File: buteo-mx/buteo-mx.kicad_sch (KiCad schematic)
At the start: 70 parts, among them J1 Conn_01x12_Pin, SW1 SW_SPST, SW10 SW_SPST, SW11 SW_SPST, SW12 SW_SPST, SW13 SW_SPST, SW14 SW_SPST, SW15 SW_SPST, SW16 SW_SPST, SW17 SW_SPST, SW18 SW_SPST, SW19 SW_SPST, SW2 SW_SPST, SW20 SW_SPST, SW21 SW_SPST, SW22 SW_SPST, SW23 SW_SPST, SW24 SW_SPST, SW25 SW_SPST, SW26 SW_SPST, SW27 SW_SPST, SW28 SW_SPST, SW29 SW_SPST, SW3 SW_SPST, SW30 SW_SPST, SW31 RotaryEncoder_Switch, SW4 SW_SPST, SW5 SW_SPST, SW6 SW_SPST, SW7 SW_SPST, SW8 SW_SPST, SW9 SW_SPST

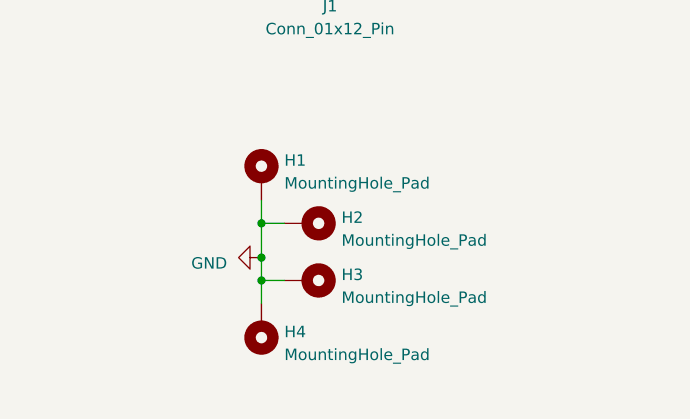
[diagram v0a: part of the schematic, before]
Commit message: Fix footprint references and 3D models
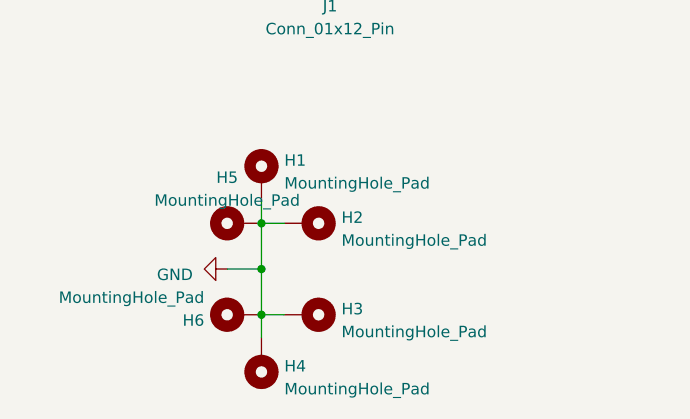
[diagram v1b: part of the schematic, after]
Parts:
- added H5, H6: MountingHole_Pad, MountingHole:MountingHole_2.2mm_M2_ISO7380_Pad_TopBottom, symbol Mechanical:MountingHole_Pad
- RZ1: footprint mcu:rp2040-zero-tht -> Pixelbreaker:rp2040-zero-tht
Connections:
- net GND: now also H5.1, H6.1
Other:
- moved on the sheet: H3, H4
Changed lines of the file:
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@@
   (junction (at 208.28 59.69) (diameter 0) (color 0 0 0 0)
   )
-  (junction (at 106.68 142.24) (diameter 0) (color 0 0 0 0)
-  )
   (junction (at 106.68 135.89) (diameter 0) (color 0 0 0 0)
   )
@@
   (junction (at 123.19 86.36) (diameter 0) (color 0 0 0 0)
   )
+  (junction (at 106.68 146.05) (diameter 0) (color 0 0 0 0)
+  )
   (junction (at 180.34 90.17) (diameter 0) (color 0 0 0 0)
   )
   (junction (at 170.18 85.09) (diameter 0) (color 0 0 0 0)
   )
-  (junction (at 106.68 139.7) (diameter 0) (color 0 0 0 0)
-  )
   (junction (at 218.44 64.77) (diameter 0) (color 0 0 0 0)
   )
@@
   (junction (at 180.34 102.87) (diameter 0) (color 0 0 0 0)
   )
+  (junction (at 106.68 140.97) (diameter 0) (color 0 0 0 0)
+  )
   (junction (at 218.44 39.37) (diameter 0) (color 0 0 0 0)
   )
@@
     (stroke (width 0) (type default))
   )
+  (wire (pts (xy 102.87 140.97) (xy 106.68 140.97))
+    (stroke (width 0) (type default))
+  )
   (wire (pts (xy 180.34 52.07) (xy 199.39 52.07))
     (stroke (width 0) (type default))
@@
     (stroke (width 0) (type default))
   )
-  (wire (pts (xy 106.68 142.24) (xy 109.22 142.24))
+  (wire (pts (xy 106.68 146.05) (xy 109.22 146.05))
     (stroke (width 0) (type default))
   )
@@
     (stroke (width 0) (type default))
   )
-  (wire (pts (xy 106.68 142.24) (xy 106.68 144.78))
-    (stroke (width 0) (type default))
-  )
   (wire (pts (xy 189.23 85.09) (xy 189.23 97.79))
     (stroke (width 0) (type default))
@@
     (stroke (width 0) (type default))
   )
+  (wire (pts (xy 106.68 140.97) (xy 106.68 146.05))
+    (stroke (width 0) (type default))
+  )
   (wire (pts (xy 170.18 34.29) (xy 170.18 46.99))
     (stroke (width 0) (type default))
@@
     (stroke (width 0) (type default))
   )
+  (wire (pts (xy 106.68 146.05) (xy 106.68 148.59))
+    (stroke (width 0) (type default))
+  )
   (wire (pts (xy 256.54 102.87) (xy 256.54 113.03))
     (stroke (width 0) (type default))
   )
-  (wire (pts (xy 106.68 135.89) (xy 106.68 139.7))
-    (stroke (width 0) (type default))
-  )
   (wire (pts (xy 160.02 77.47) (xy 180.34 77.47))
     (stroke (width 0) (type default))
@@
     (stroke (width 0) (type default))
   )
+  (wire (pts (xy 106.68 135.89) (xy 106.68 140.97))
+    (stroke (width 0) (type default))
+  )
   (wire (pts (xy 246.38 34.29) (xy 246.38 46.99))
-    (stroke (width 0) (type default))
-  )
-  (wire (pts (xy 106.68 139.7) (xy 106.68 142.24))
     (stroke (width 0) (type default))
   )
@@
     )
   )
-  (symbol (lib_id "Mechanical:MountingHole_Pad") (at 106.68 147.32 180) (unit 1)
-    (in_bom yes) (on_board yes) (dnp no) (fields_autoplaced)
-    (property "Reference" "H4" (at 109.22 147.955 0)
-      (effects (font (size 1.27 1.27)) (justify right))
-    )
-    (property "Value" "MountingHole_Pad" (at 109.22 150.495 0)
-      (effects (font (size 1.27 1.27)) (justify right))
-    )
-    (property "Footprint" "MountingHole:MountingHole_2.2mm_M2_ISO7380_Pad_TopBottom" (at 106.68 147.32 0)
-      (effects (font (size 1.27 1.27)) hide)
-    )
-    (property "Datasheet" "~" (at 106.68 147.32 0)
+  (symbol (lib_id "Mechanical:MountingHole_Pad") (at 106.68 151.13 180) (unit 1)
+    (in_bom yes) (on_board yes) (dnp no) (fields_autoplaced)
+    (property "Reference" "H4" (at 109.22 151.765 0)
+      (effects (font (size 1.27 1.27)) (justify right))
+    )
+    (property "Value" "MountingHole_Pad" (at 109.22 154.305 0)
+      (effects (font (size 1.27 1.27)) (justify right))
+    )
+    (property "Footprint" "MountingHole:MountingHole_2.2mm_M2_ISO7380_Pad_TopBottom" (at 106.68 151.13 0)
+      (effects (font (size 1.27 1.27)) hide)
+    )
+    (property "Datasheet" "~" (at 106.68 151.13 0)
       (effects (font (size 1.27 1.27)) hide)
     )
@@
     )
   )
-  (symbol (lib_id "Mechanical:MountingHole_Pad") (at 111.76 142.24 270) (unit 1)
-    (in_bom yes) (on_board yes) (dnp no) (fields_autoplaced)
-    (property "Reference" "H3" (at 115.57 141.605 90)
+  (symbol (lib_id "Mechanical:MountingHole_Pad") (at 111.76 146.05 270) (unit 1)
+    (in_bom yes) (on_board yes) (dnp no) (fields_autoplaced)
+    (property "Reference" "H3" (at 115.57 145.415 90)
       (effects (font (size 1.27 1.27)) (justify left))
     )
-    (property "Value" "MountingHole_Pad" (at 115.57 144.145 90)
+    (property "Value" "MountingHole_Pad" (at 115.57 147.955 90)
       (effects (font (size 1.27 1.27)) (justify left))
     )
-    (property "Footprint" "MountingHole:MountingHole_2.2mm_M2_ISO7380_Pad_TopBottom" (at 111.76 142.24 0)
-      (effects (font (size 1.27 1.27)) hide)
-    )
-    (property "Datasheet" "~" (at 111.76 142.24 0)
+    (property "Footprint" "MountingHole:MountingHole_2.2mm_M2_ISO7380_Pad_TopBottom" (at 111.76 146.05 0)
+      (effects (font (size 1.27 1.27)) hide)
+    )
+    (property "Datasheet" "~" (at 111.76 146.05 0)
       (effects (font (size 1.27 1.27)) hide)
     )
@@
     )
   )
+  (symbol (lib_id "Mechanical:MountingHole_Pad") (at 104.14 135.89 90) (unit 1)
+    (in_bom yes) (on_board yes) (dnp no) (fields_autoplaced)
+    (property "Reference" "H5" (at 102.87 130.81 90)
+      (effects (font (size 1.27 1.27)))
+    )
+    (property "Value" "MountingHole_Pad" (at 102.87 133.35 90)
+      (effects (font (size 1.27 1.27)))
+    )
+    (property "Footprint" "MountingHole:MountingHole_2.2mm_M2_ISO7380_Pad_TopBottom" (at 104.14 135.89 0)
+      (effects (font (size 1.27 1.27)) hide)
+    )
+    (property "Datasheet" "~" (at 104.14 135.89 0)
+      (effects (font (size 1.27 1.27)) hide)
+    )
+    (pin "1")
+    (instances
+      (project "buteo-mx"
+        (path "/cd198205-23b5-48a4-bf67-b541da52c4b6"
+          (reference "H5") (unit 1)
+        )
+      )
+    )
+  )
   (symbol (lib_id "Switch:SW_SPST") (at 175.26 34.29 0) (unit 1)
     (in_bom yes) (on_board yes) (dnp no) (fields_autoplaced)
@@
       (effects (font (size 1.27 1.27)))
     )
-    (property "Footprint" "mcu:rp2040-zero-tht" (at 109.22 30.48 0)
+    (property "Footprint" "Pixelbreaker:rp2040-zero-tht" (at 109.22 30.48 0)
       (effects (font (size 1.27 1.27)) hide)
     )
@@
     )
   )
-  (symbol (lib_id "power:GND") (at 106.68 139.7 270) (unit 1)
-    (in_bom yes) (on_board yes) (dnp no) (fields_autoplaced)
-    (property "Reference" "#PWR04" (at 100.33 139.7 0)
-      (effects (font (size 1.27 1.27)) hide)
-    )
-    (property "Value" "GND" (at 102.87 140.335 90)
-      (effects (font (size 1.27 1.27)) (justify right))
-    )
-    (property "Footprint" "" (at 106.68 139.7 0)
-      (effects (font (size 1.27 1.27)) hide)
-    )
-    (property "Datasheet" "" (at 106.68 139.7 0)
+  (symbol (lib_id "power:GND") (at 102.87 140.97 270) (unit 1)
+    (in_bom yes) (on_board yes) (dnp no) (fields_autoplaced)
+    (property "Reference" "#PWR04" (at 96.52 140.97 0)
+      (effects (font (size 1.27 1.27)) hide)
+    )
+    (property "Value" "GND" (at 99.06 141.605 90)
+      (effects (font (size 1.27 1.27)) (justify right))
+    )
+    (property "Footprint" "" (at 102.87 140.97 0)
+      (effects (font (size 1.27 1.27)) hide)
+    )
+    (property "Datasheet" "" (at 102.87 140.97 0)
       (effects (font (size 1.27 1.27)) hide)
     )
@@
         )
       )
+    )
+  )
+  (symbol (lib_id "Mechanical:MountingHole_Pad") (at 104.14 146.05 90) (unit 1)
+    (in_bom yes) (on_board yes) (dnp no)
+    (property "Reference" "H6" (at 100.33 146.685 90)
+      (effects (font (size 1.27 1.27)) (justify left))
+    )
+    (property "Value" "MountingHole_Pad" (at 100.33 144.145 90)
+      (effects (font (size 1.27 1.27)) (justify left))
+    )
+    (property "Footprint" "MountingHole:MountingHole_2.2mm_M2_ISO7380_Pad_TopBottom" (at 104.14 146.05 0)
+      (effects (font (size 1.27 1.27)) hide)
+    )
+    (property "Datasheet" "~" (at 104.14 146.05 0)
+      (effects (font (size 1.27 1.27)) hide)
+    )
+    (pin "1")
+    (instances
+      (project "buteo-mx"
+        (path "/cd198205-23b5-48a4-bf67-b541da52c4b6"
+          (reference "H6") (unit 1)
+        )
+      )

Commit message: V1 MX
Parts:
- added J2: Conn_01x04_Socket, Pixelbreaker:PinSocket_1x04_P2.54mm_Vertical, symbol Connector:Conn_01x04_Socket
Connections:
- net 3V3: now also J2.1 (Pin_1)
- net GND: now also J2.2 (Pin_2)
- net GP0 renamed SDA
- net SDA: now also J2.3 (Pin_3)
- net GP1 renamed SCL
- net SCL: now also J2.4 (Pin_4)
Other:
- moved on the sheet: H1, H2, H3, H4, H5, H6, J1
